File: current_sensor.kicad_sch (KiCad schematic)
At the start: 5 parts, among them J1 XT_60, J2 XT_60, J3 Conn_01x03_Male, U1 ACS781xLRTR-100B

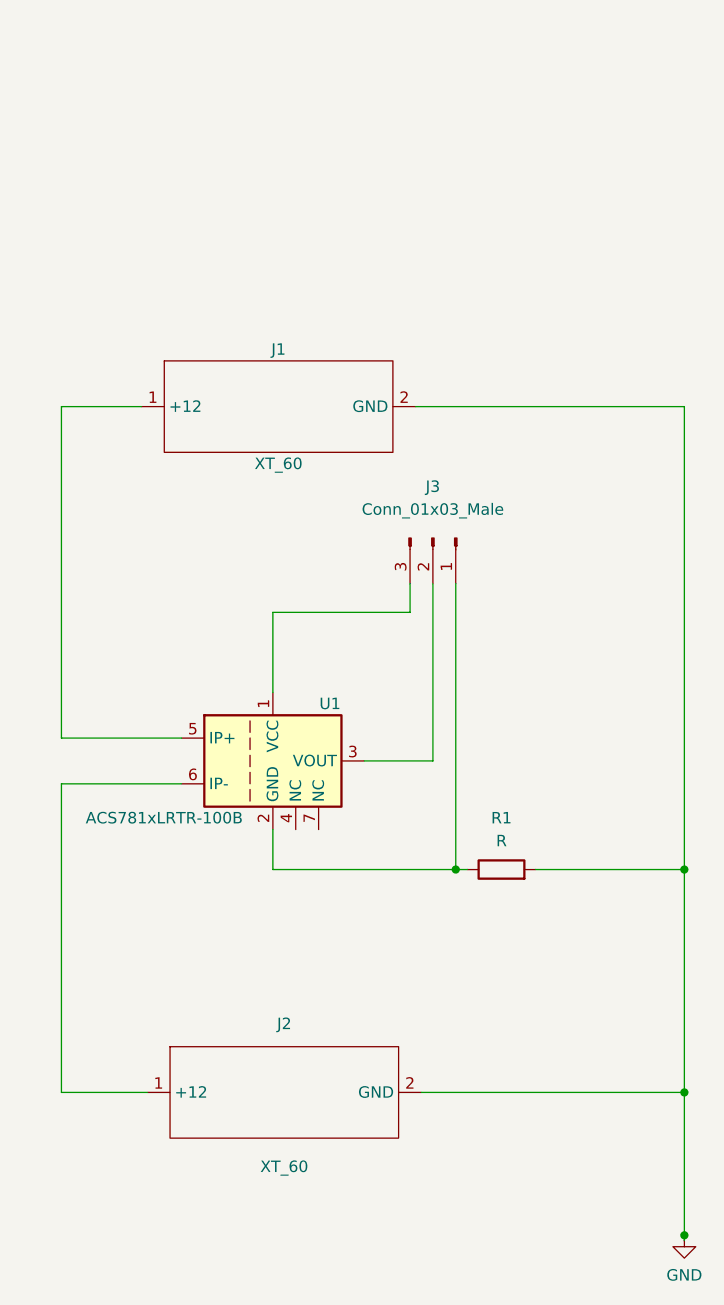
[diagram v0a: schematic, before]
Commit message: making it much smaller
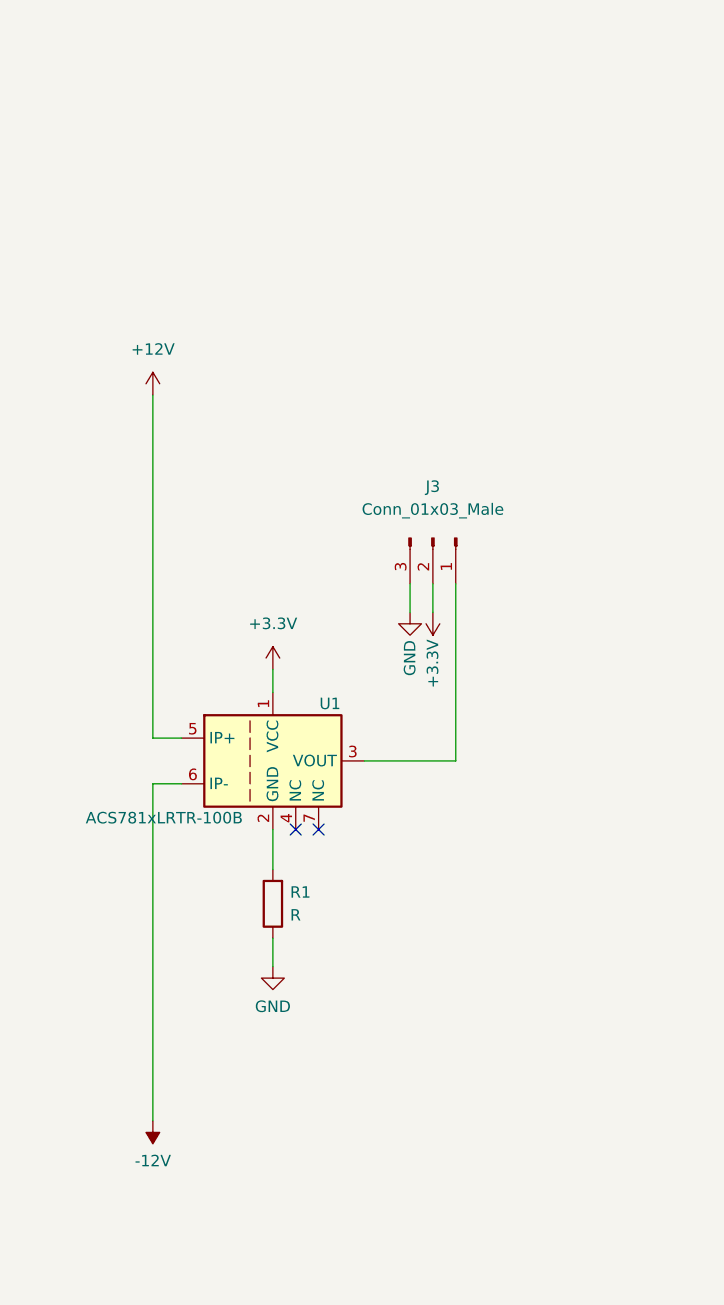
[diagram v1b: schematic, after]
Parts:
- removed J1: XT_60, Connector_AMASS:AMASS_XT60-F_1x02_P7.20mm_Vertical, symbol mtech_rmc:XT_60
- removed J2: XT_60, Connector_AMASS:AMASS_XT60-M_1x02_P7.20mm_Vertical, symbol mtech_rmc:XT_60
- J3: footprint Connector_PinHeader_2.00mm:PinHeader_1x03_P2.00mm_Vertical -> Connector_Molex:Molex_CLIK-Mate_502386-0370_1x03-1MP_P1.25mm_Horizontal
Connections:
- net GND: now also J3.3 (Pin_3), R1.1; no longer R1.2
- net at U1.3 (VOUT): now also J3.1 (Pin_1); no longer J3.2 (Pin_2)
- net +3.3V: now reaches U1.1 (VCC)
- net +3.3V: now also J3.2 (Pin_2); no longer J3.3 (Pin_3)
- net +12V: now reaches U1.5 (IP+)
- net -12V: now reaches U1.6 (IP-)
- new net: R1.2, U1.2 (GND)
- no-connect marks 0 -> 2
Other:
- moved on the sheet: R1

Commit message: make it smaller
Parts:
- removed R1: R, Resistor_SMD:R_0603_1608Metric_Pad0.98x0.95mm_HandSolder, symbol Device:R
- added C1: 0.1 uF, Capacitor_SMD:C_0603_1608Metric_Pad1.08x0.95mm_HandSolder, symbol Device:C_Small
- added C2: Cf, Capacitor_SMD:C_0603_1608Metric_Pad1.08x0.95mm_HandSolder, symbol Device:C_Small
- added R1: Rf, Resistor_SMD:R_0603_1608Metric_Pad0.98x0.95mm_HandSolder, symbol Device:R_Small
- J3: footprint Connector_Molex:Molex_CLIK-Mate_502386-0370_1x03-1MP_P1.25mm_Horizontal -> Connector_Molex:Molex_PicoBlade_53261-0371_1x03-1MP_P1.25mm_Horizontal
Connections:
- net GND is gone; now on net GNDREF: J3.3 (Pin_3)
- net +3.3V: now also C1.1
- net at J3.1 (Pin_1): now also C2.1, R1.2; no longer U1.3 (VOUT)
- net GNDREF: now reaches U1.2 (GND)
- net GNDREF: now also C1.2, C2.2
- new net: R1.1, U1.3 (VOUT)
